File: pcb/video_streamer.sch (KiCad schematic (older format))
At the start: 0 parts

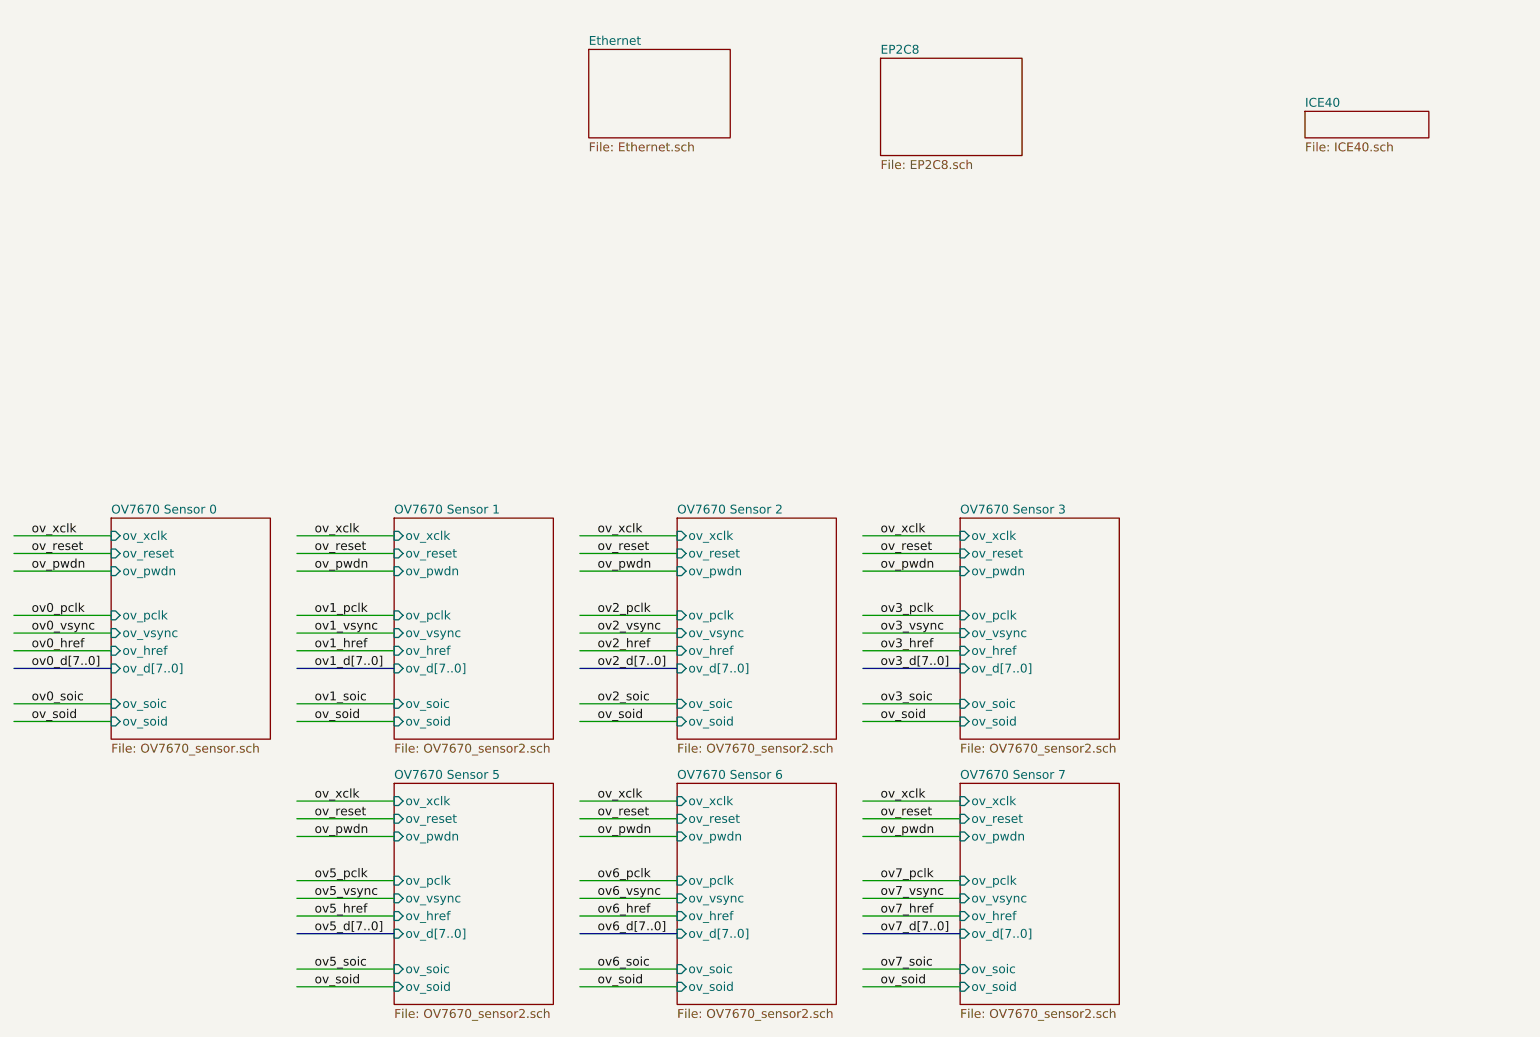
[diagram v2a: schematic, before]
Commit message: Update for latest EP2C8 symbol change.
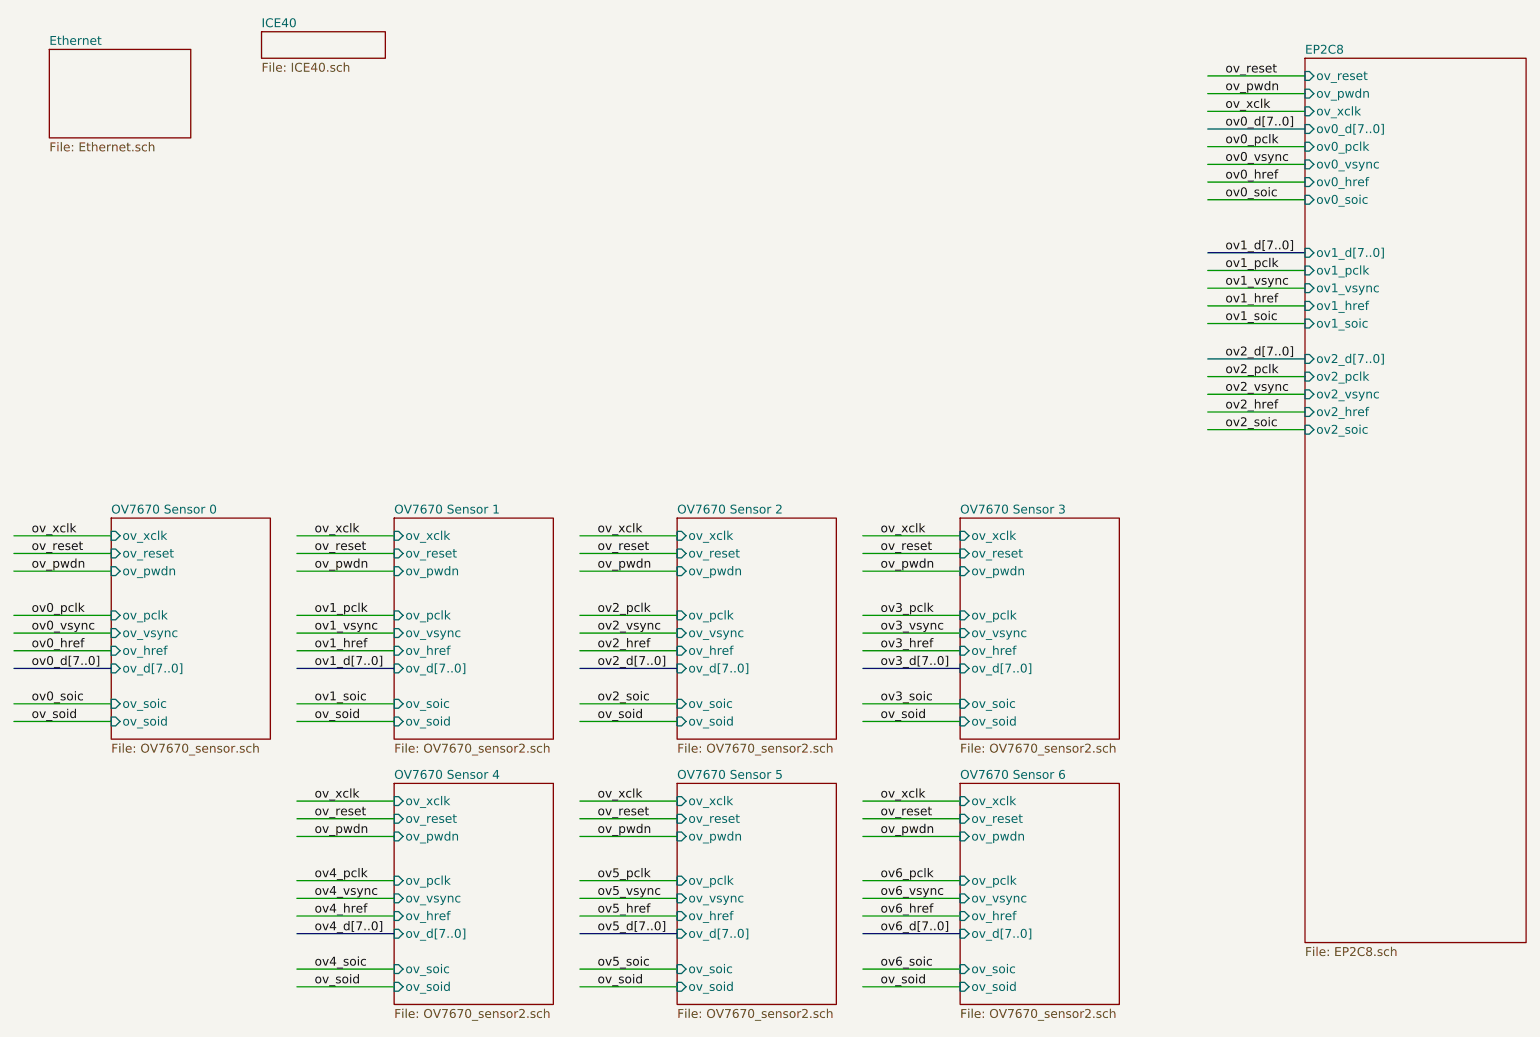
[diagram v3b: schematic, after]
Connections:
- net labels added: ov4_d[7..0], ov4_href, ov4_pclk, ov4_soic, ov4_vsync
- net labels removed: ov7_d[7..0], ov7_href, ov7_pclk, ov7_soic, ov7_vsync
- wire segments 56 -> 71
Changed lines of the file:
@@
 $EndDescr
 $Sheet
-S 4100 950  800  500
+S 1050 950  800  500
 U 5C6A4E20
 F0 "Ethernet" 50
@@
 $EndSheet
 $Sheet
-S 5750 1000 800  550
+S 8150 1000 1250 5000
 U 5C9A920A
 F0 "EP2C8" 50
 F1 "EP2C8.sch" 50
+F2 "ov_reset" I L 8150 1100 50
+F3 "ov_pwdn" I L 8150 1200 50
+F4 "ov_xclk" I L 8150 1300 50
+F5 "ov0_d[7..0]" I L 8150 1400 50
+F6 "ov0_pclk" I L 8150 1500 50
+F7 "ov0_vsync" I L 8150 1600 50
+F8 "ov0_href" I L 8150 1700 50
+F9 "ov0_soic" I L 8150 1800 50
+F10 "ov1_d[7..0]" I L 8150 2100 50
+F11 "ov1_pclk" I L 8150 2200 50
+F12 "ov1_vsync" I L 8150 2300 50
+F13 "ov1_href" I L 8150 2400 50
+F14 "ov1_soic" I L 8150 2500 50
+F15 "ov2_d[7..0]" I L 8150 2700 50
+F16 "ov2_pclk" I L 8150 2800 50
+F17 "ov2_vsync" I L 8150 2900 50
+F18 "ov2_href" I L 8150 3000 50
+F19 "ov2_soic" I L 8150 3100 50
 $EndSheet
 $Sheet
@@
 S 3000 5100 900  1250
 U 5C9CA93A
-F0 "OV7670 Sensor 5" 50
+F0 "OV7670 Sensor 4" 50
 F1 "OV7670_sensor2.sch" 50
 F2 "ov_pclk" I L 3000 5650 50
@@
 	3000 5650 2450 5650
 Text Label 2550 5650 0    50   ~ 0
-ov5_pclk
+ov4_pclk
 Wire Wire Line
 	3000 5750 2450 5750
 Text Label 2550 5750 0    50   ~ 0
-ov5_vsync
+ov4_vsync
 Wire Wire Line
 	3000 5850 2450 5850
 Text Label 2550 5850 0    50   ~ 0
-ov5_href
+ov4_href
 Wire Bus Line
 	3000 5950 2450 5950
 Text Label 2550 5950 0    50   ~ 0
-ov5_d[7..0]
+ov4_d[7..0]
 Wire Wire Line
 	3000 6150 2450 6150
 Text Label 2550 6150 0    50   ~ 0
-ov5_soic
+ov4_soic
 Wire Wire Line
 	3000 6250 2450 6250
@@
 S 4600 5100 900  1250
 U 5C9CA957
-F0 "OV7670 Sensor 6" 50
+F0 "OV7670 Sensor 5" 50
 F1 "OV7670_sensor2.sch" 50
 F2 "ov_pclk" I L 4600 5650 50
@@
 	4600 5650 4050 5650
 Text Label 4150 5650 0    50   ~ 0
-ov6_pclk
+ov5_pclk
 Wire Wire Line
 	4600 5750 4050 5750
 Text Label 4150 5750 0    50   ~ 0
-ov6_vsync
+ov5_vsync
 Wire Wire Line
 	4600 5850 4050 5850
 Text Label 4150 5850 0    50   ~ 0
-ov6_href
+ov5_href
 Wire Bus Line
 	4600 5950 4050 5950
 Text Label 4150 5950 0    50   ~ 0
-ov6_d[7..0]
+ov5_d[7..0]
 Wire Wire Line
 	4600 6150 4050 6150
 Text Label 4150 6150 0    50   ~ 0
-ov6_soic
+ov5_soic
 Wire Wire Line
 	4600 6250 4050 6250
@@
 S 6200 5100 900  1250
 U 5C9CA974
-F0 "OV7670 Sensor 7" 50
+F0 "OV7670 Sensor 6" 50
 F1 "OV7670_sensor2.sch" 50
 F2 "ov_pclk" I L 6200 5650 50
@@
 	6200 5650 5650 5650
 Text Label 5750 5650 0    50   ~ 0
-ov7_pclk
+ov6_pclk
 Wire Wire Line
 	6200 5750 5650 5750
 Text Label 5750 5750 0    50   ~ 0
-ov7_vsync
+ov6_vsync
 Wire Wire Line
 	6200 5850 5650 5850
 Text Label 5750 5850 0    50   ~ 0
-ov7_href
+ov6_href
 Wire Bus Line
 	6200 5950 5650 5950
 Text Label 5750 5950 0    50   ~ 0
-ov7_d[7..0]
+ov6_d[7..0]
 Wire Wire Line
 	6200 6150 5650 6150
 Text Label 5750 6150 0    50   ~ 0
-ov7_soic
+ov6_soic
 Wire Wire Line
 	6200 6250 5650 6250
@@
 ov_soid
 $Sheet
-S 8150 1300 700  150
+S 2250 850  700  150
 U 5C67FC17
 F0 "ICE40" 50
 F1 "ICE40.sch" 50
 $EndSheet
+Wire Wire Line
+	8150 1300 7600 1300
+Text Label 7700 1300 0    50   ~ 0
+ov_xclk
+Text Label 7700 1100 0    50   ~ 0
+ov_reset
+Wire Wire Line
+	8150 1200 7600 1200
+Text Label 7700 1200 0    50   ~ 0
+ov_pwdn
+Wire Wire Line
+	8150 1100 7600 1100
+Wire Bus Line
+	8150 1400 7600 1400
+Text Label 7700 1400 0    50   ~ 0
+ov0_d[7..0]
+Wire Wire Line
+	8150 1500 7600 1500
+Text Label 7700 1500 0    50   ~ 0
+ov0_pclk
+Wire Wire Line
+	8150 1600 7600 1600
+Text Label 7700 1600 0    50   ~ 0
+ov0_vsync
+Wire Wire Line
+	8150 1700 7600 1700
+Text Label 7700 1700 0    50   ~ 0
+ov0_href
+Wire Wire Line
+	8150 1800 7600 1800
+Text Label 7700 1800 0    50   ~ 0
+ov0_soic
+Wire Wire Line
+	8150 2200 7600 2200
+Text Label 7700 2200 0    50   ~ 0
+ov1_pclk
+Wire Wire Line
+	8150 2300 7600 2300
+Text Label 7700 2300 0    50   ~ 0
+ov1_vsync
+Wire Wire Line
+	8150 2400 7600 2400
+Text Label 7700 2400 0    50   ~ 0
+ov1_href
+Wire Bus Line
+	8150 2100 7600 2100
+Text Label 7700 2100 0    50   ~ 0
+ov1_d[7..0]
+Wire Wire Line
+	8150 2500 7600 2500
+Text Label 7700 2500 0    50   ~ 0
+ov1_soic
+Wire Wire Line
+	8150 2800 7600 2800
+Text Label 7700 2800 0    50   ~ 0
+ov2_pclk
+Wire Wire Line
+	8150 2900 7600 2900
+Text Label 7700 2900 0    50   ~ 0
+ov2_vsync
+Wire Wire Line
+	8150 3000 7600 3000
+Text Label 7700 3000 0    50   ~ 0
+ov2_href
+Wire Bus Line
+	8150 2700 7600 2700
+Text Label 7700 2700 0    50   ~ 0
+ov2_d[7..0]
+Wire Wire Line
+	8150 3100 7600 3100
+Text Label 7700 3100 0    50   ~ 0
+ov2_soic
 $EndSCHEMATC
